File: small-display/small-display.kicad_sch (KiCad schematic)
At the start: 46 parts, among them J1 2047110001, J2 Micro_SD_Card_Det, J5 F32D-1A7Y1-21040, U1 TPD4EUSB30, U2 74LVC1G07SE-7, U3 RT9742GGJ5, U4 PAM2804AAB010, U5 USB2412-DZK, U6 NLVVHC1G04DFT1G, U7 M24M01-DFDW6TP, Y1 ECS-240-8-33-AGN-TR

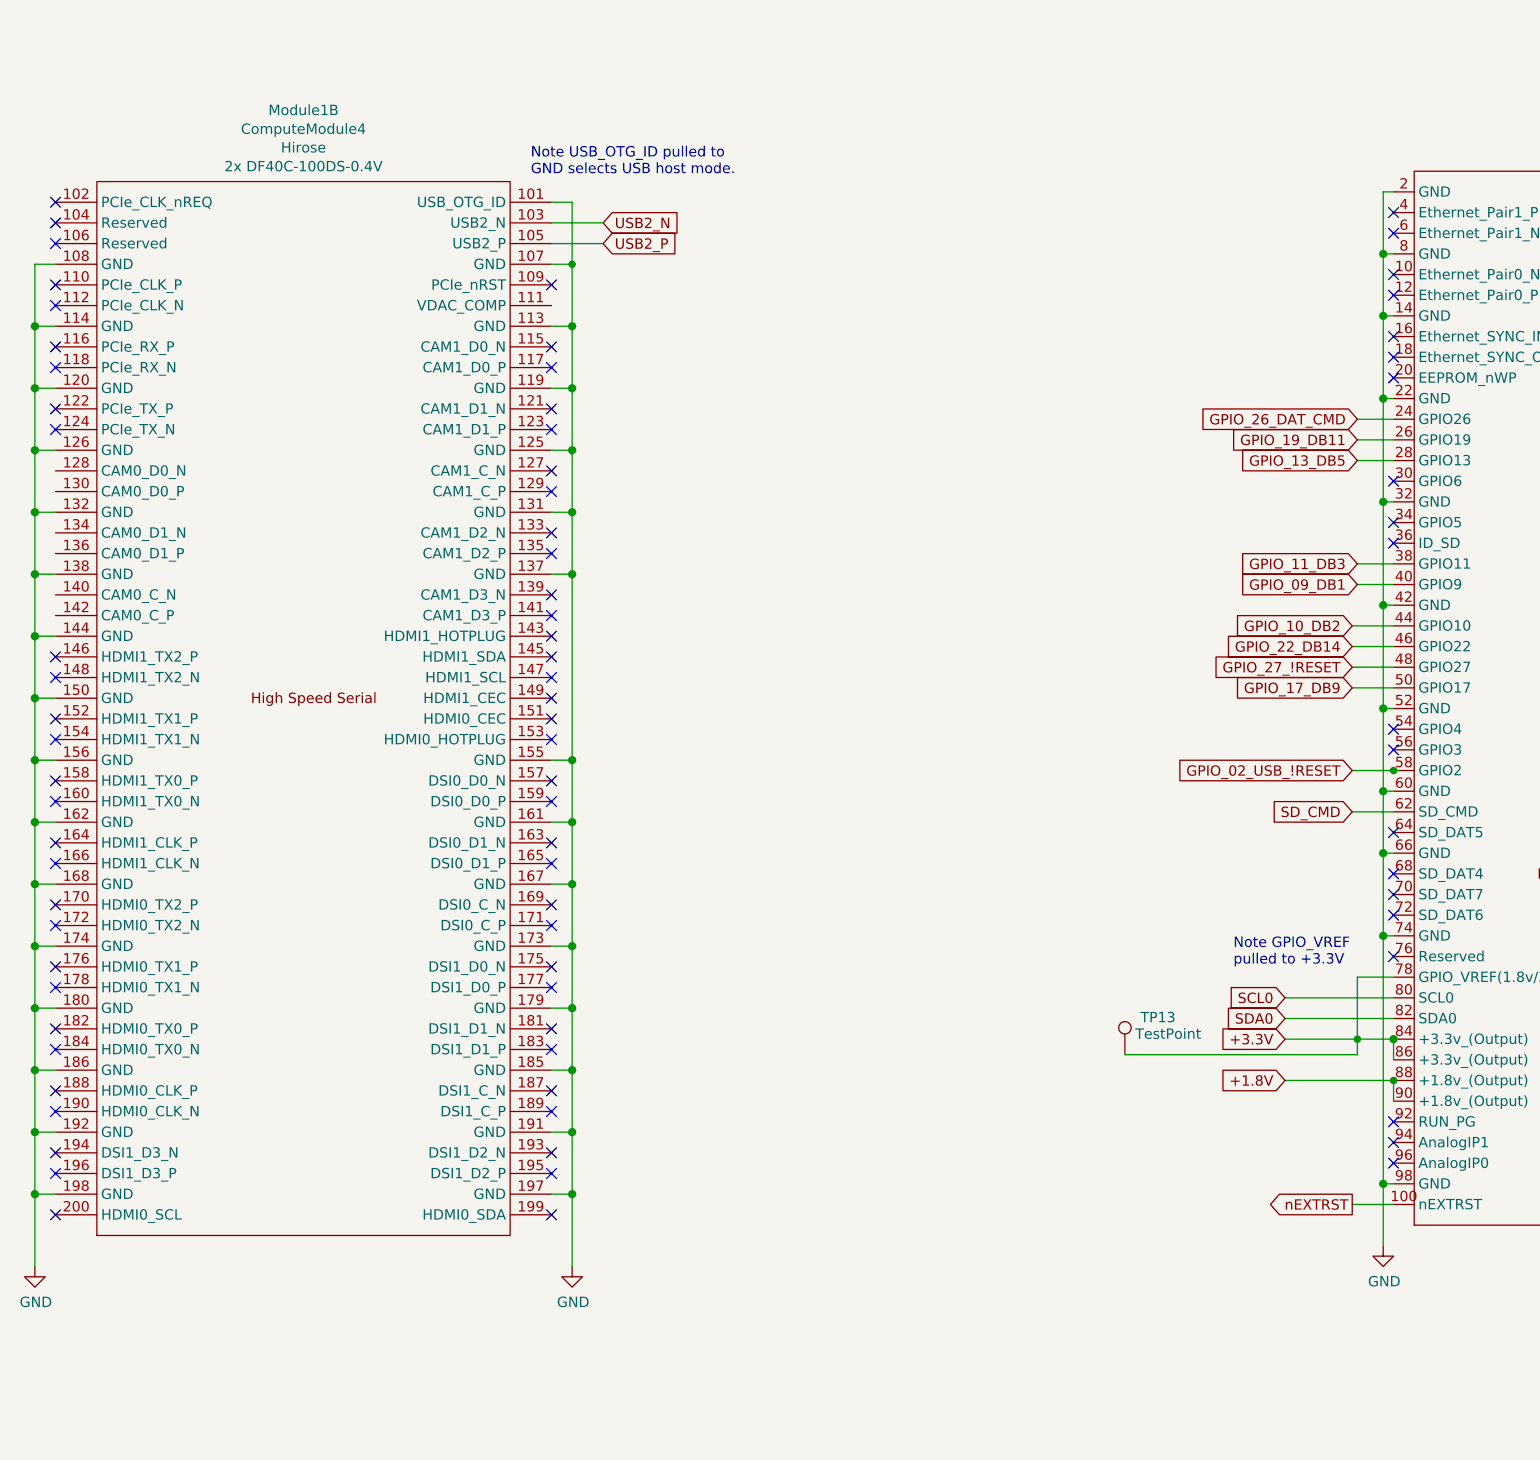
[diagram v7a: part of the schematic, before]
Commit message: Added 4.7k I2C pullup resistors.
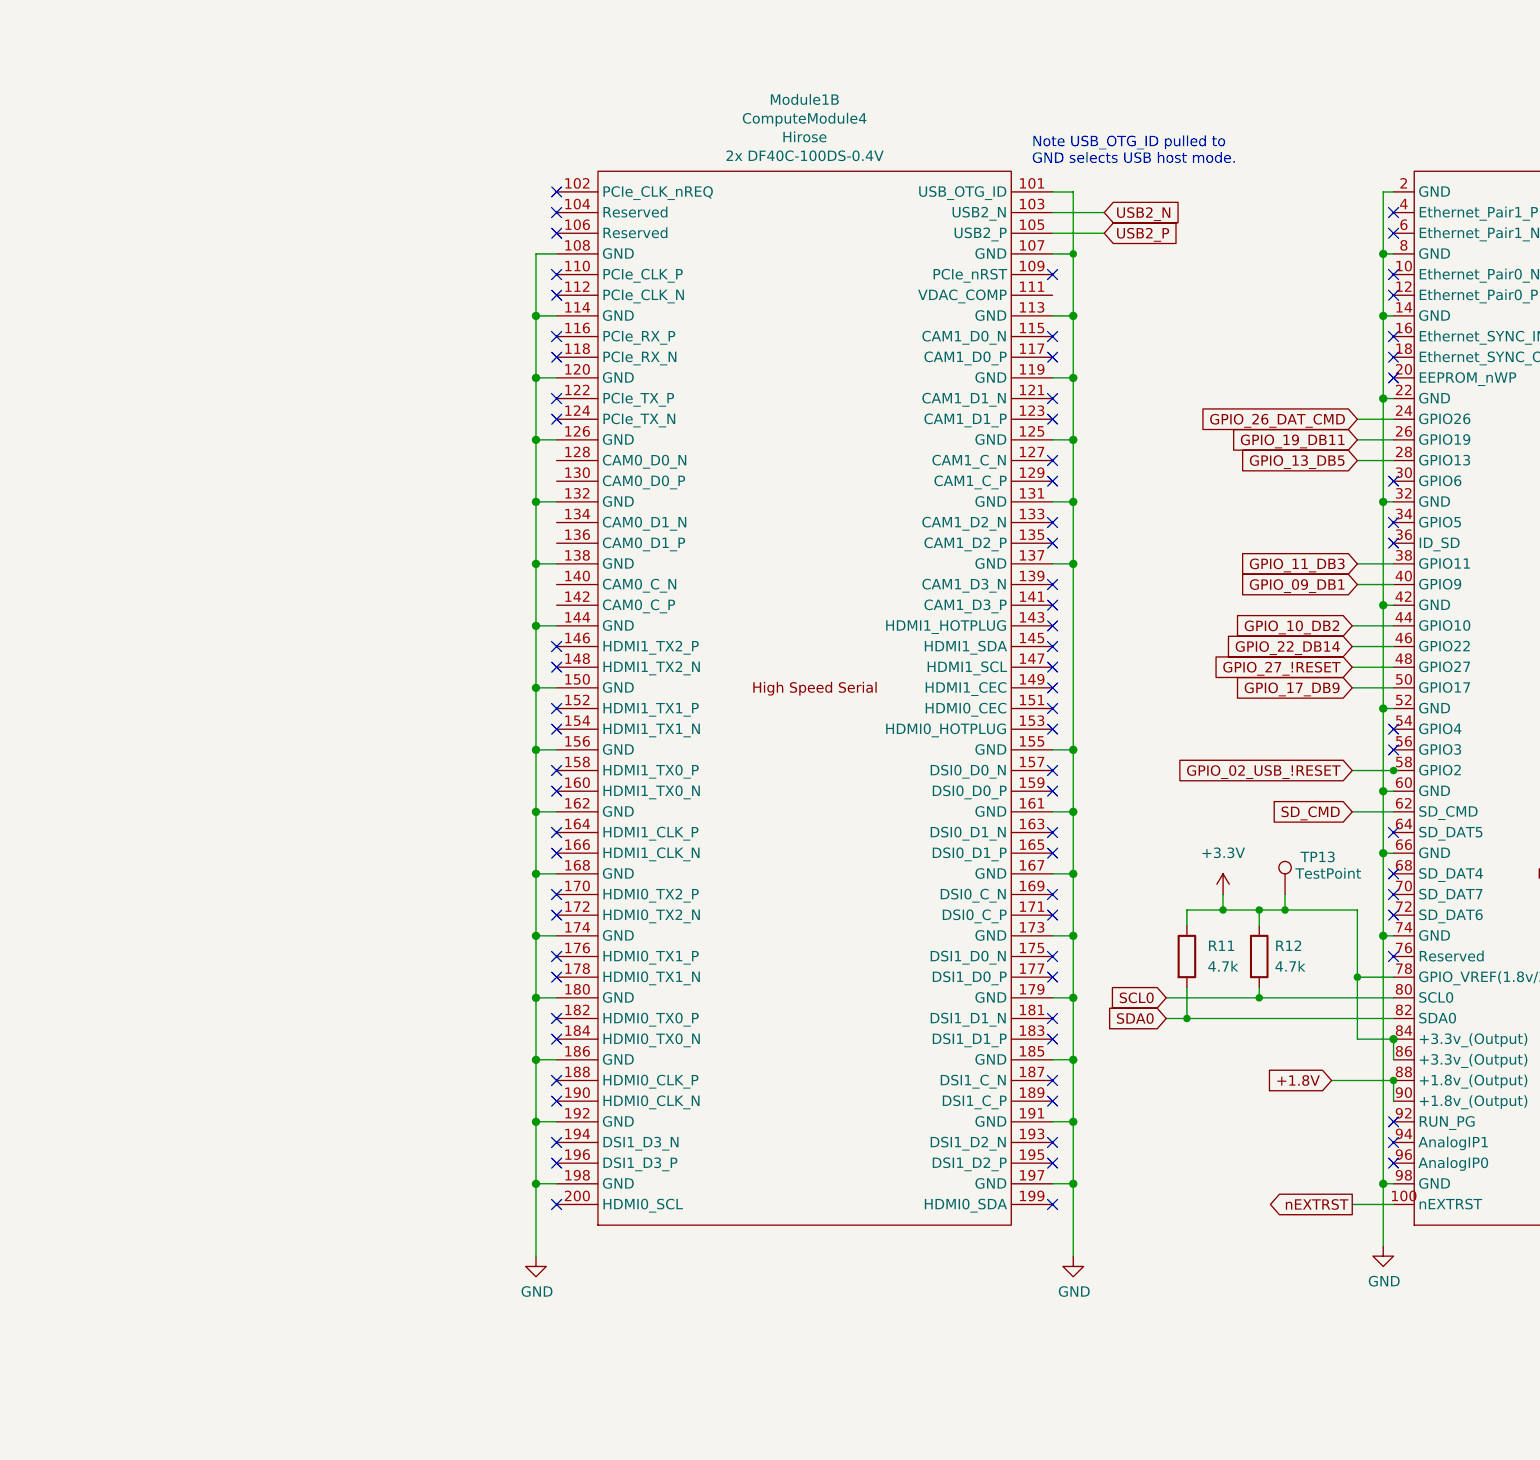
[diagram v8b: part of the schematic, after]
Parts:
- added R11, R12: 4.7k, Resistor_SMD:R_0603_1608Metric, symbol Device:R
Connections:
- net +3.3V: now also R11.1, R12.1
- net SCL0: now also R12.2
- net SDA0: now also R11.2
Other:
- note removed: "Note GPIO_VREF pulled to +3.3V"
- moved on the sheet: Module1B, TP13
